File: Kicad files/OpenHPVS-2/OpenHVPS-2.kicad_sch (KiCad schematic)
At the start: 69 parts, among them J1 Conn_01x03_Male, J2 Conn_01x03_Male, Q1 FQT7N10, Q2 BC846A, Q3 MMDT3906, U1 MAX6008AEUR+T, U2 74HC14, U3 MAX4162, U4 CD14538BM

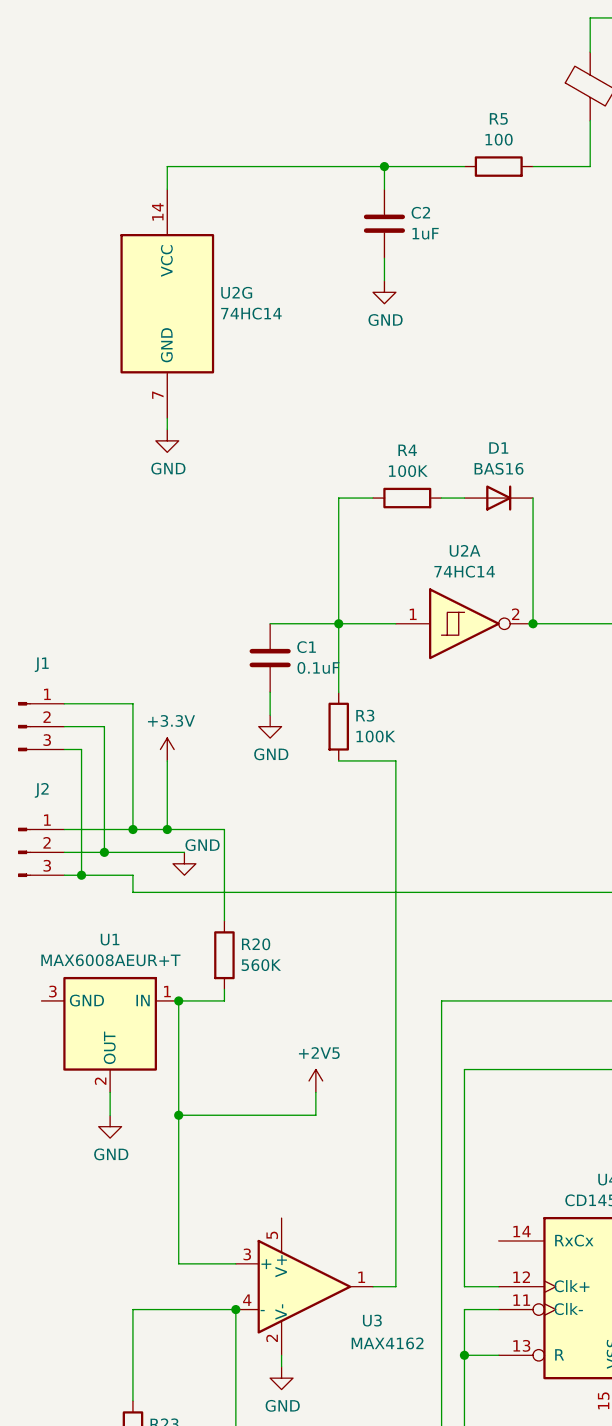
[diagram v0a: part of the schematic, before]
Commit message: Forgot the supply to the opamp - added. changed a capacitor value
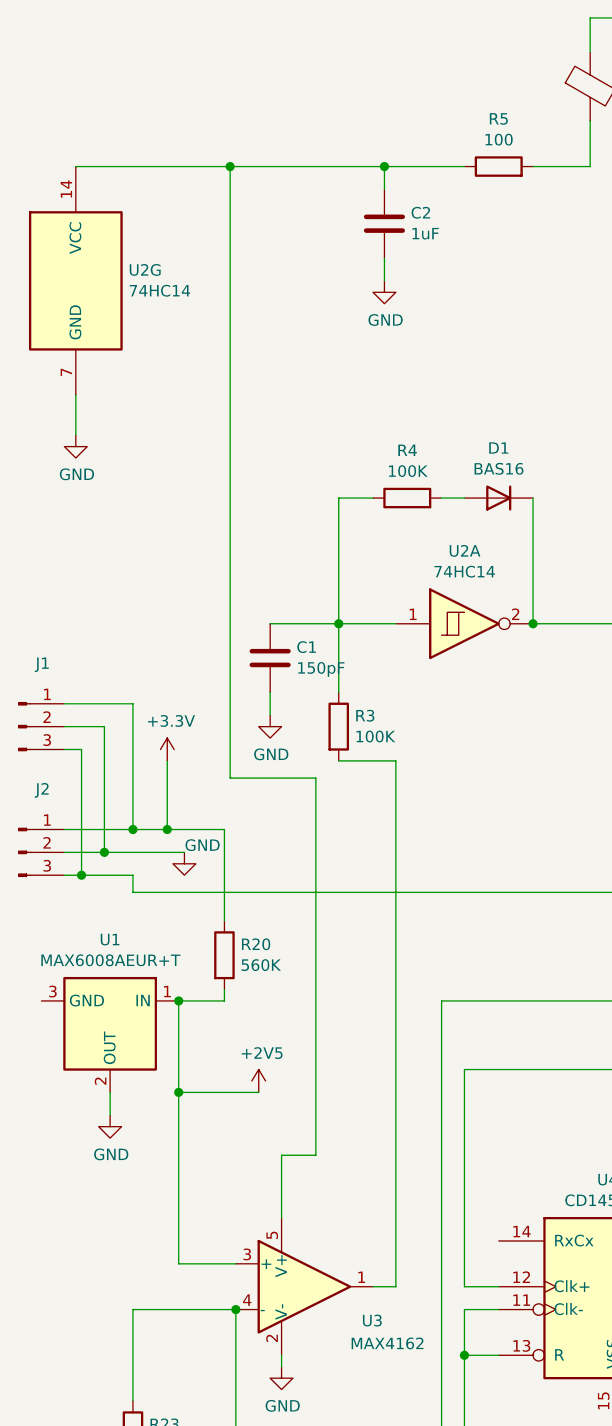
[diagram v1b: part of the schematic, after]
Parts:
- C1: value 0.1uF -> 150pF
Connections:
- net at C2.1, R5.1, U2.14 (VCC): now also U3.5 (V+)
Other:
- moved on the sheet: U2G
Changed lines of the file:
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@@
   (junction (at 34.29 111.125) (diameter 1.016) (color 0 0 0 0))
   (junction (at 35.56 130.175) (diameter 1.016) (color 0 0 0 0))
-  (junction (at 35.56 142.875) (diameter 1.016) (color 0 0 0 0))
+  (junction (at 35.56 140.335) (diameter 1.016) (color 0 0 0 0))
+  (junction (at 41.275 37.465) (diameter 1.016) (color 0 0 0 0))
   (junction (at 41.91 164.465) (diameter 1.016) (color 0 0 0 0))
   (junction (at 53.34 88.265) (diameter 1.016) (color 0 0 0 0))
@@
     (stroke (width 0) (type solid) (color 0 0 0 0))
   )
+  (wire (pts (xy 24.13 37.465) (xy 41.275 37.465))
+    (stroke (width 0) (type solid) (color 0 0 0 0))
+  )
+  (wire (pts (xy 24.13 62.865) (xy 24.13 67.31))
+    (stroke (width 0) (type solid) (color 0 0 0 0))
+  )
   (wire (pts (xy 24.765 102.235) (xy 24.765 116.205))
     (stroke (width 0) (type solid) (color 0 0 0 0))
@@
     (stroke (width 0) (type solid) (color 0 0 0 0))
   )
-  (wire (pts (xy 34.29 37.465) (xy 34.29 40.005))
-    (stroke (width 0) (type solid) (color 0 0 0 0))
-  )
-  (wire (pts (xy 34.29 65.405) (xy 34.29 66.675))
-    (stroke (width 0) (type solid) (color 0 0 0 0))
-  )
   (wire (pts (xy 34.29 103.505) (xy 34.29 111.125))
     (stroke (width 0) (type solid) (color 0 0 0 0))
@@
     (stroke (width 0) (type solid) (color 0 0 0 0))
   )
-  (wire (pts (xy 35.56 130.175) (xy 35.56 142.875))
-    (stroke (width 0) (type solid) (color 0 0 0 0))
-  )
-  (wire (pts (xy 35.56 142.875) (xy 35.56 159.385))
+  (wire (pts (xy 35.56 130.175) (xy 35.56 140.335))
+    (stroke (width 0) (type solid) (color 0 0 0 0))
+  )
+  (wire (pts (xy 35.56 140.335) (xy 35.56 159.385))
     (stroke (width 0) (type solid) (color 0 0 0 0))
   )
@@
     (stroke (width 0) (type solid) (color 0 0 0 0))
   )
+  (wire (pts (xy 41.275 37.465) (xy 58.42 37.465))
+    (stroke (width 0) (type solid) (color 0 0 0 0))
+  )
+  (wire (pts (xy 41.275 105.41) (xy 41.275 37.465))
+    (stroke (width 0) (type solid) (color 0 0 0 0))
+  )
   (wire (pts (xy 41.91 159.385) (xy 35.56 159.385))
     (stroke (width 0) (type solid) (color 0 0 0 0))
@@
     (stroke (width 0) (type solid) (color 0 0 0 0))
   )
+  (wire (pts (xy 44.45 140.335) (xy 35.56 140.335))
+    (stroke (width 0) (type solid) (color 0 0 0 0))
+  )
   (wire (pts (xy 45.72 88.265) (xy 53.34 88.265))
     (stroke (width 0) (type solid) (color 0 0 0 0))
@@
     (stroke (width 0) (type solid) (color 0 0 0 0))
   )
+  (wire (pts (xy 46.99 147.32) (xy 50.8 147.32))
+    (stroke (width 0) (type solid) (color 0 0 0 0))
+  )
+  (wire (pts (xy 46.99 154.305) (xy 46.99 147.32))
+    (stroke (width 0) (type solid) (color 0 0 0 0))
+  )
   (wire (pts (xy 46.99 170.815) (xy 46.99 169.545))
     (stroke (width 0) (type solid) (color 0 0 0 0))
   )
-  (wire (pts (xy 50.8 140.335) (xy 50.8 142.875))
-    (stroke (width 0) (type solid) (color 0 0 0 0))
-  )
-  (wire (pts (xy 50.8 142.875) (xy 35.56 142.875))
+  (wire (pts (xy 50.8 105.41) (xy 41.275 105.41))
+    (stroke (width 0) (type solid) (color 0 0 0 0))
+  )
+  (wire (pts (xy 50.8 147.32) (xy 50.8 105.41))
     (stroke (width 0) (type solid) (color 0 0 0 0))
   )
@@
   )
   (wire (pts (xy 57.15 161.925) (xy 59.69 161.925))
-    (stroke (width 0) (type solid) (color 0 0 0 0))
-  )
-  (wire (pts (xy 58.42 37.465) (xy 34.29 37.465))
     (stroke (width 0) (type solid) (color 0 0 0 0))
   )
@@
     )
   )
-  (symbol (lib_id "power:+2V5") (at 50.8 140.335 0) (unit 1)
-    (in_bom yes) (on_board yes)
-    (property "Reference" "#PWR08" (id 0) (at 50.8 144.145 0)
-      (effects (font (size 1.27 1.27)) hide)
-    )
-    (property "Value" "+2V5" (id 1) (at 51.1683 136.0106 0))
-    (property "Footprint" "" (id 2) (at 50.8 140.335 0)
-      (effects (font (size 1.27 1.27)) hide)
-    )
-    (property "Datasheet" "" (id 3) (at 50.8 140.335 0)
+  (symbol (lib_id "power:+2V5") (at 44.45 140.335 0) (unit 1)
+    (in_bom yes) (on_board yes)
+    (property "Reference" "#PWR08" (id 0) (at 44.45 144.145 0)
+      (effects (font (size 1.27 1.27)) hide)
+    )
+    (property "Value" "+2V5" (id 1) (at 44.8183 136.0106 0))
+    (property "Footprint" "" (id 2) (at 44.45 140.335 0)
+      (effects (font (size 1.27 1.27)) hide)
+    )
+    (property "Datasheet" "" (id 3) (at 44.45 140.335 0)
       (effects (font (size 1.27 1.27)) hide)
     )
@@
     )
   )
+  (symbol (lib_id "power:GND") (at 24.13 67.31 0) (unit 1)
+    (in_bom yes) (on_board yes)
+    (property "Reference" "#PWR03" (id 0) (at 24.13 73.66 0)
+      (effects (font (size 1.27 1.27)) hide)
+    )
+    (property "Value" "GND" (id 1) (at 24.257 71.7042 0))
+    (property "Footprint" "" (id 2) (at 24.13 67.31 0)
+      (effects (font (size 1.27 1.27)) hide)
+    )
+    (property "Datasheet" "" (id 3) (at 24.13 67.31 0)
+      (effects (font (size 1.27 1.27)) hide)
+    )
+  )
   (symbol (lib_id "power:GND") (at 27.94 142.875 0) (unit 1)
     (in_bom yes) (on_board yes)
@@
     )
     (property "Datasheet" "" (id 3) (at 30.48 182.245 0)
-      (effects (font (size 1.27 1.27)) hide)
-    )
-  )
-  (symbol (lib_id "power:GND") (at 34.29 66.675 0) (unit 1)
-    (in_bom yes) (on_board yes)
-    (property "Reference" "#PWR03" (id 0) (at 34.29 73.025 0)
-      (effects (font (size 1.27 1.27)) hide)
-    )
-    (property "Value" "GND" (id 1) (at 34.417 71.0692 0))
-    (property "Footprint" "" (id 2) (at 34.29 66.675 0)
-      (effects (font (size 1.27 1.27)) hide)
-    )
-    (property "Datasheet" "" (id 3) (at 34.29 66.675 0)
       (effects (font (size 1.27 1.27)) hide)
     )
@@
       (effects (font (size 1.27 1.27)) (justify left))
     )
-    (property "Value" "0.1uF" (id 1) (at 48.641 93.218 0)
+    (property "Value" "150pF" (id 1) (at 48.641 93.218 0)
       (effects (font (size 1.27 1.27)) (justify left))
     )
@@
       (effects (font (size 1.27 1.27)) hide)
     )
-    (property "Datasheet" "https://www.digikey.com/en/products/detail/tdk-corporation/C2012X7T2E104K125AA/2733184" (id 3) (at 45.72 92.075 0)
+    (property "Datasheet" "https://www.digikey.com/en/products/detail/w%C3%BCrth-elektronik/885012207111/9346002" (id 3) (at 45.72 92.075 0)
       (effects (font (size 1.27 1.27)) hide)
     )
@@
     )
   )
-  (symbol (lib_id "74xx:74HC14") (at 34.29 52.705 0) (unit 7)
-    (in_bom yes) (on_board yes)
-    (property "Reference" "U2" (id 0) (at 40.132 51.5366 0)
-      (effects (font (size 1.27 1.27)) (justify left))
-    )
-    (property "Value" "74HC14" (id 1) (at 40.132 53.848 0)
-      (effects (font (size 1.27 1.27)) (justify left))
-    )
-    (property "Footprint" "Package_SO:SOIC-14_3.9x8.7mm_P1.27mm" (id 2) (at 34.29 52.705 0)
-      (effects (font (size 1.27 1.27)) hide)
-    )
-    (property "Datasheet" "https://www.digikey.com/en/products/detail/texas-instruments/CD74HC14M96/390309" (id 3) (at 34.29 52.705 0)
+  (symbol (lib_id "74xx:74HC14") (at 24.13 50.165 0) (unit 7)
+    (in_bom yes) (on_board yes)
+    (property "Reference" "U2" (id 0) (at 29.972 48.9966 0)
+      (effects (font (size 1.27 1.27)) (justify left))
+    )
+    (property "Value" "74HC14" (id 1) (at 29.972 51.308 0)
+      (effects (font (size 1.27 1.27)) (justify left))
+    )
+    (property "Footprint" "Package_SO:SOIC-14_3.9x8.7mm_P1.27mm" (id 2) (at 24.13 50.165 0)
+      (effects (font (size 1.27 1.27)) hide)
+    )
+    (property "Datasheet" "https://www.digikey.com/en/products/detail/texas-instruments/CD74HC14M96/390309" (id 3) (at 24.13 50.165 0)
       (effects (font (size 1.27 1.27)) hide)
     )
@@
     )
     (path "/00000000-0000-0000-0000-0000600fa622"
-      (reference "C1") (unit 1) (value "0.1uF") (footprint "Capacitor_SMD:C_0805_2012Metric")
+      (reference "C1") (unit 1) (value "150pF") (footprint "Capacitor_SMD:C_0805_2012Metric")
     )
     (path "/00000000-0000-0000-0000-0000600aa140"
